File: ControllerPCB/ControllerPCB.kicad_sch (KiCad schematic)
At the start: 109 parts, among them J1 Conn_02x40_Row_Letter_First, SW1 SW_SPDT, U2 STM32F439ZITx, Y2 WE-XTAL_CFPX-218

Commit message: rev 0.1 - Redid the GPIO pinouts and removed the CLRs. - Split the 80 pin conn into two 40 pin conns - Added conn and pinouts for SWD - Added conn and pinouts for USB_FS over USB Micro B - Added conn for the MIDI Controls and Piezo pickup
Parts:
- removed J1: Conn_02x40_Row_Letter_First, symbol Connector_Generic:Conn_02x40_Row_Letter_First
- removed R10, R11, R12, R13, R14, R15, R16, R17, R18, R19, R20, R21, R22, R23, R24, R25, R26, R27, R28, R29, R30, R31, R32, R33, R34, R35, R36, R37, R38, R39, R4, R40, R41, R42, R43, R44, R45, R46, R47, R48, R49, R5, R50, R51, R52, R53, R54, R55, R56, R57, R58, R59, R6, R60, R61, R62, R63, R64, R65, R66, R67, R68, R69, R7, R70, R71, R72, R73, R74, R75, R76, R77, R78, R79, R8, R80, R81, R9: 10k, Resistor_SMD:R_1206_3216Metric, symbol Device:R
- added J1: 2x4 Pickup Conn, symbol Connector_Generic:Conn_02x04_Odd_Even
- added J3: USB_B_Micro, symbol Connector:USB_B_Micro
- added J4: 10-pin SWD Connector, symbol Connector_Generic:Conn_02x05_Odd_Even
- added J5: 2x8 MIDI Controls Conn, symbol Connector_Generic:Conn_02x08_Odd_Even
- added J6: 2x20 Conn_1, symbol Connector_Generic:Conn_02x20_Odd_Even
- added J7: 2x20 Conn_2, symbol Connector_Generic:Conn_02x20_Odd_Even
- R2: value 10k -> 33k; footprint Resistor_SMD:R_1206_3216Metric -> (none)
- R3: value 10k -> 82k; footprint Resistor_SMD:R_1206_3216Metric -> (none)
- U2: value STM32F439ZITx -> STM32F439ZIT6
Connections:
- net +3.3V: now also J4.1 (Pin_1), J5.10 (Pin_10), J5.12 (Pin_12), J5.14 (Pin_14), J5.16 (Pin_16), J5.8 (Pin_8); no longer C15.1, C16.1, C19.1, C20.1, FB1.1, U2.32 (VREF+), U2.33 (VDDA)
- net GND: now also R3.2, J1.2 (Pin_2), J1.4 (Pin_4), J1.6 (Pin_6), J1.8 (Pin_8), J3.5 (GND), J4.3 (Pin_3), J4.5 (Pin_5), J4.9 (Pin_9), J5.11 (Pin_11), J5.13 (Pin_13), J5.15 (Pin_15), J5.7 (Pin_7), J5.9 (Pin_9)
- net NRST: now also J4.10 (Pin_10)
- net PE2: now also J7.3 (Pin_3)
- net PE3: now also J7.5 (Pin_5)
- net PE4: now also J7.7 (Pin_7)
- net PE5: now also J7.9 (Pin_9)
- net PE6: now also J7.11 (Pin_11)
- net PE7: now also J7.13 (Pin_13)
- net PF0: now also J7.31 (Pin_31)
- net PF1: now also J7.33 (Pin_33)
- net PF11: now also J7.14 (Pin_14)
- net PF12: now also J7.16 (Pin_16)
- net PF13: now also J7.18 (Pin_18)
- net PF14: now also J7.20 (Pin_20)
- net PF15: now also J7.22 (Pin_22)
- net PF2: now also J7.35 (Pin_35)
- net PG0: now also J7.24 (Pin_24)
- net PG1: now also J7.26 (Pin_26)
- net PG2: now also J7.28 (Pin_28)
- net PG3: now also J7.30 (Pin_30)
- net PG4: now also J7.32 (Pin_32)
- net PG5: now also J7.34 (Pin_34)
- net PG6: now also J7.36 (Pin_36)
- net PG7: now also J7.38 (Pin_38)
- net PG8: now also J7.40 (Pin_40)
- net VBUS_SENSE: now reaches R2.2
- net VBUS_SENSE: now also R3.1, U2.101 (PA9)
- net HSE_IN: now reaches C21.1, U2.23 (PH0), Y2.1
- net HSE_OUT: now reaches C22.1, U2.24 (PH1), Y2.3
- net PD14: now reaches U2.85 (PD14)
- net PD14: now also J6.40 (Pin_40)
- net PB1: now reaches U2.47 (PB1)
- net PB1: now also J6.7 (Pin_7); no longer R3.1
- net PC14: now reaches U2.8 (PC14)
- net PC14: now also J6.10 (Pin_10)
- net PD0: now reaches U2.114 (PD0)
- net PD0: now also J6.14 (Pin_14)
- net at R2.1: now also J3.1 (VBUS); no longer U2.46 (PB0)
- net PB11: now reaches U2.70 (PB11)
- net PB11: now also J6.11 (Pin_11)
- net PD1: now reaches U2.115 (PD1)
- net PD1: now also J6.16 (Pin_16)
- net PD3: now reaches U2.117 (PD3)
- net PD3: now also J6.20 (Pin_20)
- net PC13: now reaches U2.7 (PC13)
- net PC13: now also J6.8 (Pin_8)
- net PC0: now reaches U2.26 (PC0)
- net PC0: now also J6.21 (Pin_21)
- net PD12: now reaches U2.81 (PD12)
- net PD12: now also J6.36 (Pin_36)
- net PB10: now reaches U2.69 (PB10)
- net PB10: now also J6.9 (Pin_9)
- net PC11: now reaches U2.112 (PC11)
- net PC11: now also J6.4 (Pin_4)
- net PC4: now reaches U2.44 (PC4)
- net PC4: now also J6.29 (Pin_29)
- net PD4: now reaches U2.118 (PD4)
- net PD4: now also J6.22 (Pin_22)
- net PC5: now reaches U2.45 (PC5)
- net PC5: now also J6.31 (Pin_31)
- net PD5: now reaches U2.119 (PD5)
- net PD5: now also J6.24 (Pin_24)
- net PD2: now reaches U2.116 (PD2)
- net PD2: now also J6.18 (Pin_18)
- net PD10: now reaches U2.79 (PD10)
- net PD10: now also J6.32 (Pin_32)
- net PC2: now reaches U2.28 (PC2)
- net PC2: now also J6.25 (Pin_25)
- net PC12: now reaches U2.113 (PC12)
- net PC12: now also J6.6 (Pin_6)
- net PD15: now reaches U2.86 (PD15)
- net PD15: now also J7.1 (Pin_1)
- net PC1: now reaches U2.27 (PC1)
- net PC1: now also J6.23 (Pin_23)
- net PC6: now reaches U2.96 (PC6)
- net PC6: now also J6.33 (Pin_33)
- net PC3: now reaches U2.29 (PC3)
- net PC3: now also J6.27 (Pin_27)
- net PB14: now reaches U2.75 (PB14)
- net PB14: now also J6.17 (Pin_17)
- net SWO: now reaches U2.133 (PB3)
- net SWO: now also J4.6 (Pin_6)
- net PD11: now reaches U2.80 (PD11)
- net PD11: now also J6.34 (Pin_34)
- net PD8: now reaches U2.77 (PD8)
- net PD8: now also J6.28 (Pin_28)
- net PD9: now reaches U2.78 (PD9)
- net PD9: now also J6.30 (Pin_30)
- net PC8: now reaches U2.98 (PC8)
- net PC8: now also J6.37 (Pin_37)
- net PC9: now reaches U2.99 (PC9)
- net PC9: now also J6.39 (Pin_39)
- net PB15: now reaches U2.76 (PB15)
- net PB15: now also J6.19 (Pin_19)
- net PB13: now reaches U2.74 (PB13)
- net PB13: now also J6.15 (Pin_15)
- net PC10: now reaches U2.111 (PC10)
- net PC10: now also J6.2 (Pin_2)
- net PD13: now reaches U2.82 (PD13)
- net PD13: now also J6.38 (Pin_38)
- net PA8: now reaches U2.100 (PA8)
- net PA8: now also J6.1 (Pin_1)
- net PA10: now reaches U2.102 (PA10)
- net PA10: now also J6.3 (Pin_3)
- net D-: now reaches U2.103 (PA11)
- net D-: now also J3.2 (D-)
- net D+: now reaches U2.104 (PA12)
- net D+: now also J3.3 (D+)
- net SWDIO: now reaches U2.105 (PA13)
- net SWDIO: now also J4.2 (Pin_2)
- net SWDCLK: now reaches U2.109 (PA14)
- net SWDCLK: now also J4.4 (Pin_4)
- net PA15: now reaches U2.110 (PA15)
- net PA15: now also J6.5 (Pin_5)
- net PD6: now reaches U2.122 (PD6)
- net PD6: now also J6.26 (Pin_26)
- net ADC_String_1: now reaches U2.34 (PA0)
- net ADC_String_1: now also J1.1 (Pin_1)
- net ADC_String_2: now reaches U2.35 (PA1)
- net ADC_String_2: now also J1.3 (Pin_3)
- net ADC_String_3: now reaches U2.36 (PA2)
- net ADC_String_3: now also J1.5 (Pin_5)
- net ADC_String_4: now reaches U2.37 (PA3)
- net ADC_String_4: now also J1.7 (Pin_7)
- net ADC_Octave: now reaches U2.40 (PA4)
- net ADC_Octave: now also J5.1 (Pin_1)
- net ADC_Mod: now reaches U2.41 (PA5)
- net ADC_Mod: now also J5.2 (Pin_2)
- net ADC_Bend: now reaches U2.42 (PA6)
- net ADC_Bend: now also J5.3 (Pin_3), J5.4 (Pin_4)
- net ADC_MIDI_Ch: now reaches U2.43 (PA7)
- net ADC_MIDI_Ch: now also J5.5 (Pin_5)
- net PE12: now reaches U2.65 (PE12)
- net PE12: now also J7.23 (Pin_23)
- net PE13: now reaches U2.66 (PE13)
- net PE13: now also J7.25 (Pin_25)
- net PE14: now reaches U2.67 (PE14)
- net PE14: now also J7.27 (Pin_27)
- net PE15: now reaches U2.68 (PE15)
- net PE15: now also J7.29 (Pin_29)
- net PB12: now reaches U2.73 (PB12)
- net PB12: now also J6.13 (Pin_13)
- net PC15: now reaches U2.9 (PC15)
- net PC15: now also J6.12 (Pin_12)
- net PC7: now reaches U2.97 (PC7)
- net PC7: now also J6.35 (Pin_35)
- net ADC3_IN14 renamed PF4
- net PF4: now also J7.39 (Pin_39)
- net ADC3_IN15 renamed PF5
- net PF5: now also J7.2 (Pin_2)
- net ADC3_IN4 renamed PF6
- net PF6: now also J7.4 (Pin_4)
- net ADC3_IN5 renamed PF7
- net PF7: now also J7.6 (Pin_6)
- net ADC3_IN6 renamed PF8
- net PF8: now also J7.8 (Pin_8)
- net ADC3_IN7 renamed PF9
- net PF9: now also J7.10 (Pin_10)
- net ADC3_IN8 renamed PF10
- net PF10: now also J7.12 (Pin_12)
- net ADC3_IN9 renamed PF3
- net PF3: now also J7.37 (Pin_37)
- net PE0: no longer names the net of U2.141 (PE0)
- net PE1: no longer names the net of U2.142 (PE1)
- net PG10: no longer names the net of U2.125 (PG10)
- net PG11: no longer names the net of U2.126 (PG11)
- net PG12: no longer names the net of U2.127 (PG12)
- net PG13: no longer names the net of U2.128 (PG13)
- net PG14: no longer names the net of U2.129 (PG14)
- net PG15: no longer names the net of U2.132 (PG15)
- net PG9: no longer names the net of U2.124 (PG9)
- net String1 renamed PE8
- net PE8: now also J7.15 (Pin_15)
- net String2 renamed PE9
- net PE9: now also J7.17 (Pin_17)
- net String3 renamed PE10
- net PE10: now also J7.19 (Pin_19)
- net String4 renamed PE11
- net PE11: now also J7.21 (Pin_21)
- new net +3.3VA: C15.1, C16.1, C19.1, C20.1, FB1.1, U2.32 (VREF+), U2.33 (VDDA)
- new net ADC_Thresh: U2.46 (PB0)
- no-connect marks 4 -> 22
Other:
- note added: "Many GND and +3.3V here since each ADC MIDI control input voltage is varied using a 100kOhm potentiometer"
- note added: "add net lables to everything? do global lables act as net lables?"
- note added: "needa figure this shit out. will do soon"

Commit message: Redid the power supply schematic. Controller now powered from the 5V supply from the usb VBUS. Also added EMD suppression TVS diode to the VBUS line to avoid any possible voltage surge.
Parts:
- removed R2: 33k, symbol Device:R
- removed R3: 82k, symbol Device:R
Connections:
- net VBUS: now reaches J3.1 (VBUS)
- net VBUS_SENSE: no longer names the net of U2.101 (PA9)
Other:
- removed sheet Amplitude_Detection
- note removed: "add net lables to everything? do global lables act as net lables?"
- moved on the sheet: J3

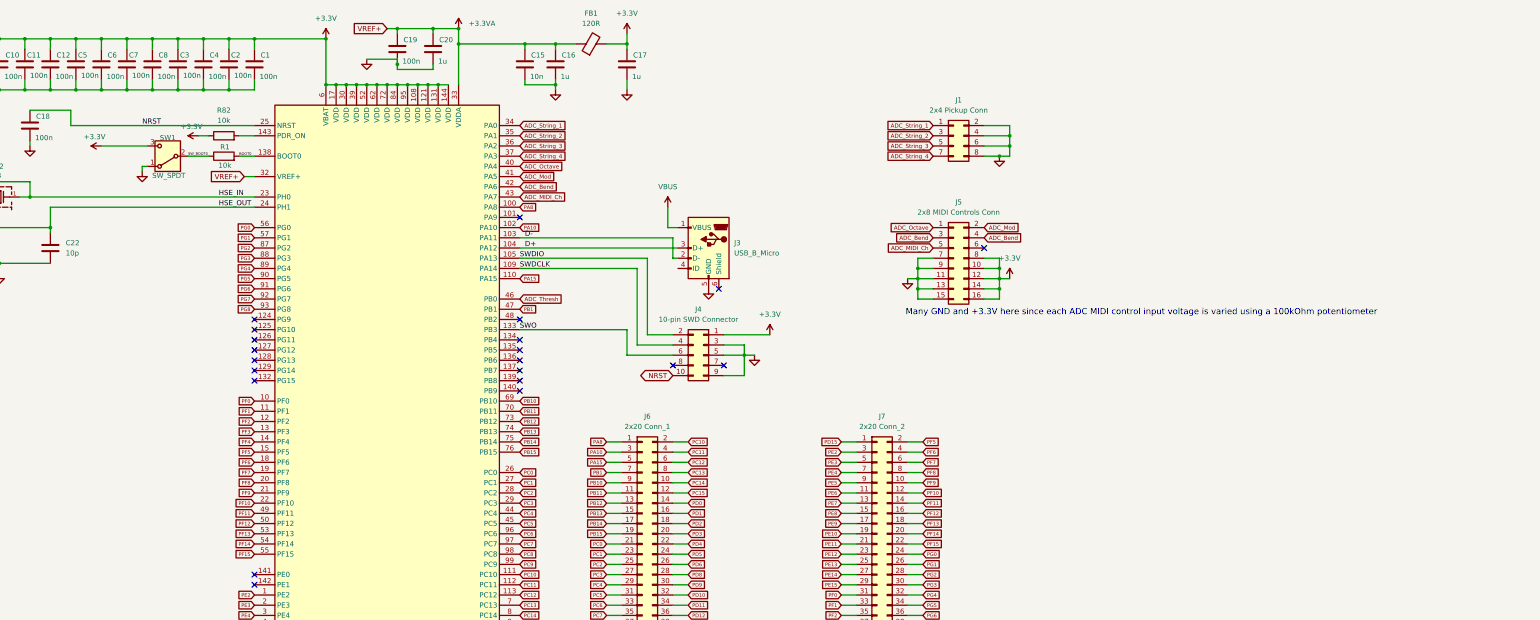
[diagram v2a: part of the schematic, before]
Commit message: Split the MIDI controls connector into 5 3-pin connectors. Added an extra MIDI controls connector in case we want to add another control. Added the 1x4 string output connector.
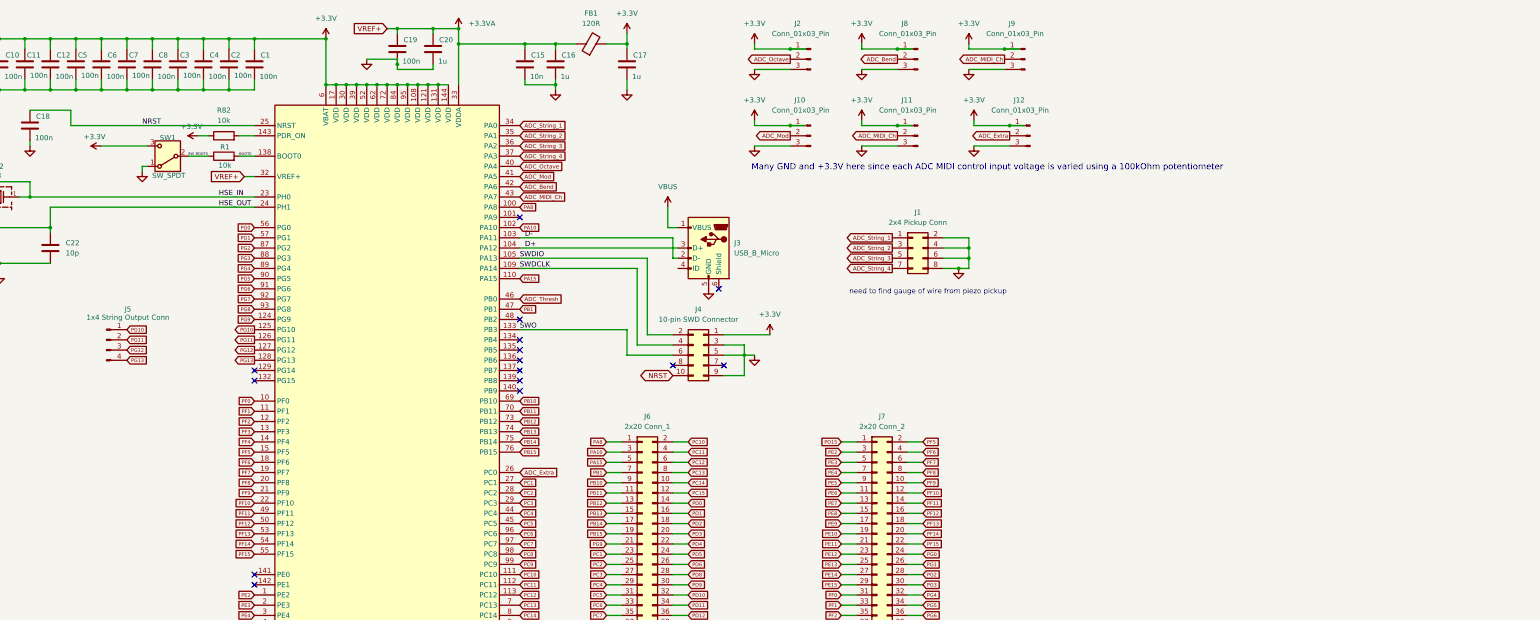
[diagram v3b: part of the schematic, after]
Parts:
- removed J5: 2x8 MIDI Controls Conn, symbol Connector_Generic:Conn_02x08_Odd_Even
- added J10, J11, J12, J2, J8, J9: Conn_01x03_Pin, symbol Connector:Conn_01x03_Pin
- added J5: 1x4 String Output Conn, symbol Connector:Conn_01x04_Pin
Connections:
- net +3.3V: now also J10.1 (Pin_1), J11.1 (Pin_1), J12.1 (Pin_1), J2.1 (Pin_1), J8.1 (Pin_1), J9.1 (Pin_1)
- net ADC_Bend: now also J8.2 (Pin_2)
- net ADC_MIDI_Ch: now also J11.2 (Pin_2), J9.2 (Pin_2)
- net ADC_Mod: now also J10.2 (Pin_2)
- net ADC_Octave: now also J2.2 (Pin_2)
- net GND: now also J10.3 (Pin_3), J11.3 (Pin_3), J12.3 (Pin_3), J2.3 (Pin_3), J8.3 (Pin_3), J9.3 (Pin_3)
- net PG9: now reaches U2.124 (PG9)
- net PG9: now also J6.21 (Pin_21)
- net PG10: now reaches U2.125 (PG10)
- net PG10: now also J5.1 (Pin_1)
- net PG11: now reaches U2.126 (PG11)
- net PG11: now also J5.2 (Pin_2)
- net PG12: now reaches U2.127 (PG12)
- net PG12: now also J5.3 (Pin_3)
- net PG13: now reaches U2.128 (PG13)
- net PG13: now also J5.4 (Pin_4)
- net PC0 renamed ADC_Extra
- net ADC_Extra: now also J12.2 (Pin_2); no longer J6.21 (Pin_21)
- no-connect marks 22 -> 16
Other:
- note added: "need to find gauge of wire from piezo pickup"

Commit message: Updated many things.
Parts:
- added D2: D-_TVS, symbol Device:D_TVS
- added D3: D+_TVS, symbol Device:D_TVS
- added D4: VBUS_TVS, symbol Device:D_TVS
- added R7: 33k, symbol Device:R
- added R8: 82k, symbol Device:R
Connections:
- net ADC_Bend: now also J9.2 (Pin_2); no longer J8.2 (Pin_2)
- net ADC_MIDI_Ch: now also J10.2 (Pin_2); no longer J11.2 (Pin_2), J9.2 (Pin_2)
- net ADC_Mod: now also J8.2 (Pin_2); no longer J10.2 (Pin_2)
- net ADC_Thresh: now also J11.2 (Pin_2)
- net D+: now also D3.2 (A2)
- net D-: now also D2.2 (A2)
- net GND: now also D2.1 (A1), D3.1 (A1), D4.1 (A1), R8.2
- net VBUS_Sense: now reaches U2.101 (PA9)
- net VBUS_Sense: now also R7.2, R8.1
- net PD7: now reaches U2.123 (PD7)
- net PD7: now also J6.28 (Pin_28)
- net PD8 renamed UART_TX
- net UART_TX: no longer J6.28 (Pin_28)
- net VBUS: no longer names the net of J3.1 (VBUS)
- net VBUS: now also D4.2 (A2), R7.1
- no-connect marks 16 -> 15
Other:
- added sheet Amplitude Detection (amp_detection.kicad_sch)
- added sheet MIDI OUT (midi_out.kicad_sch)
- note added: "23-0022111031-ND"
- note added: "75869-107LF"
- note added: "75869-332LF - TBC"
- note added: "ESD351DPYR"
- note added: "FTSH-105-01-F-D-K"
- note added: "PESD5V5C1BLYL"
- note added: "WM2746-ND"
- moved on the sheet: J1, J2, J3, J4
